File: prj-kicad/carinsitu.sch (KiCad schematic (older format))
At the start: 25 parts, among them P1 BAT, P2 MOT, U1 ESP32, U2 MIC2860, X1 40MHz

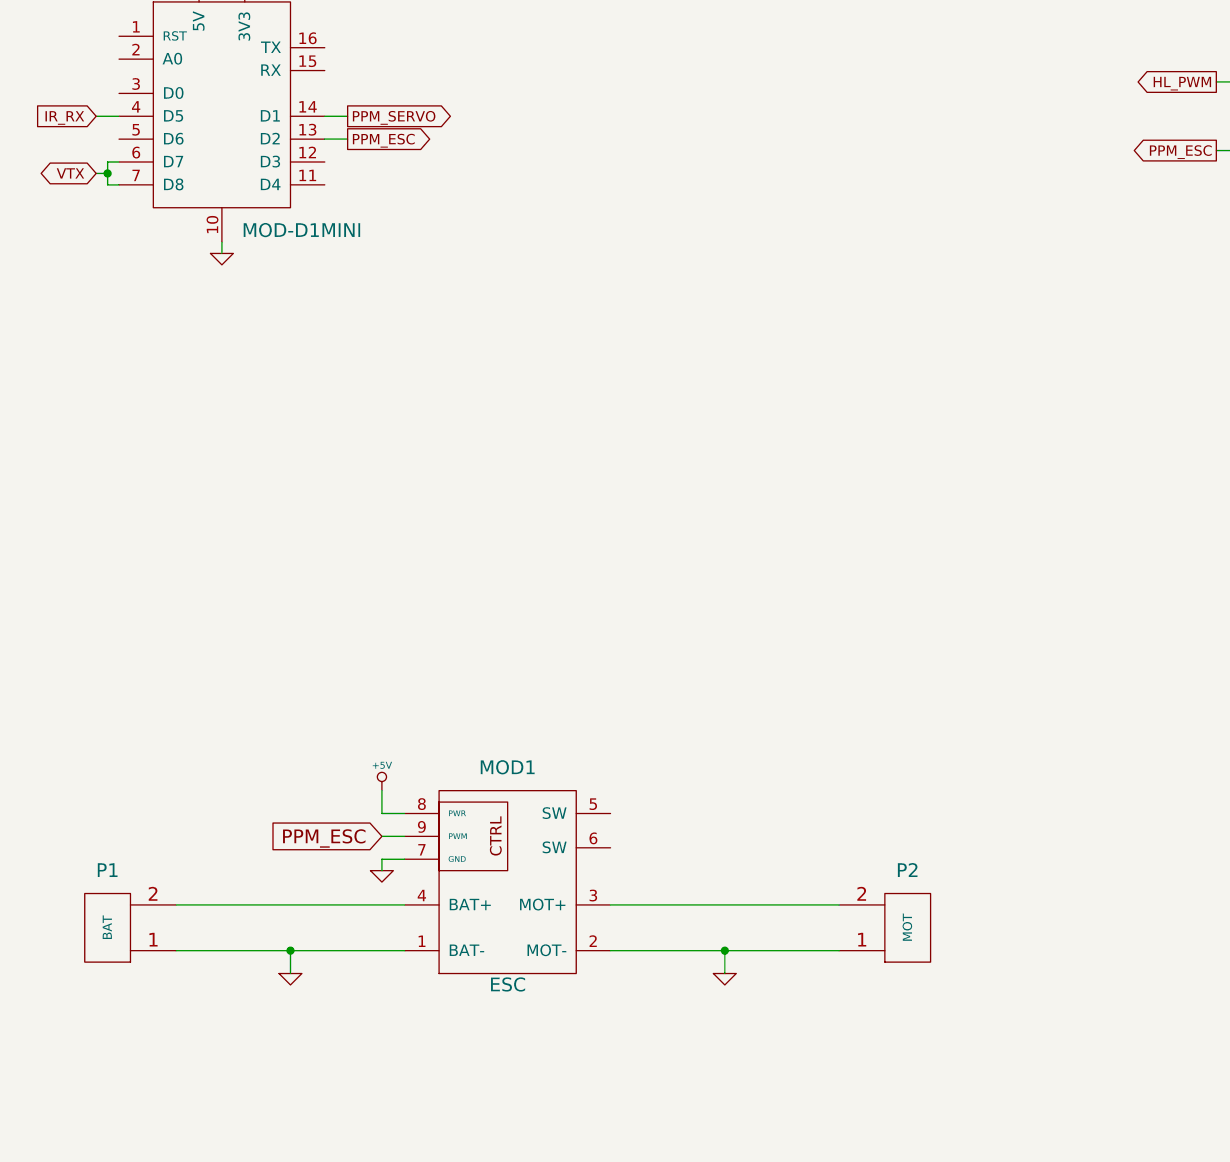
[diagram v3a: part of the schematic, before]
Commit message: = ADD: Insert a slide switch to connect power (on / off)
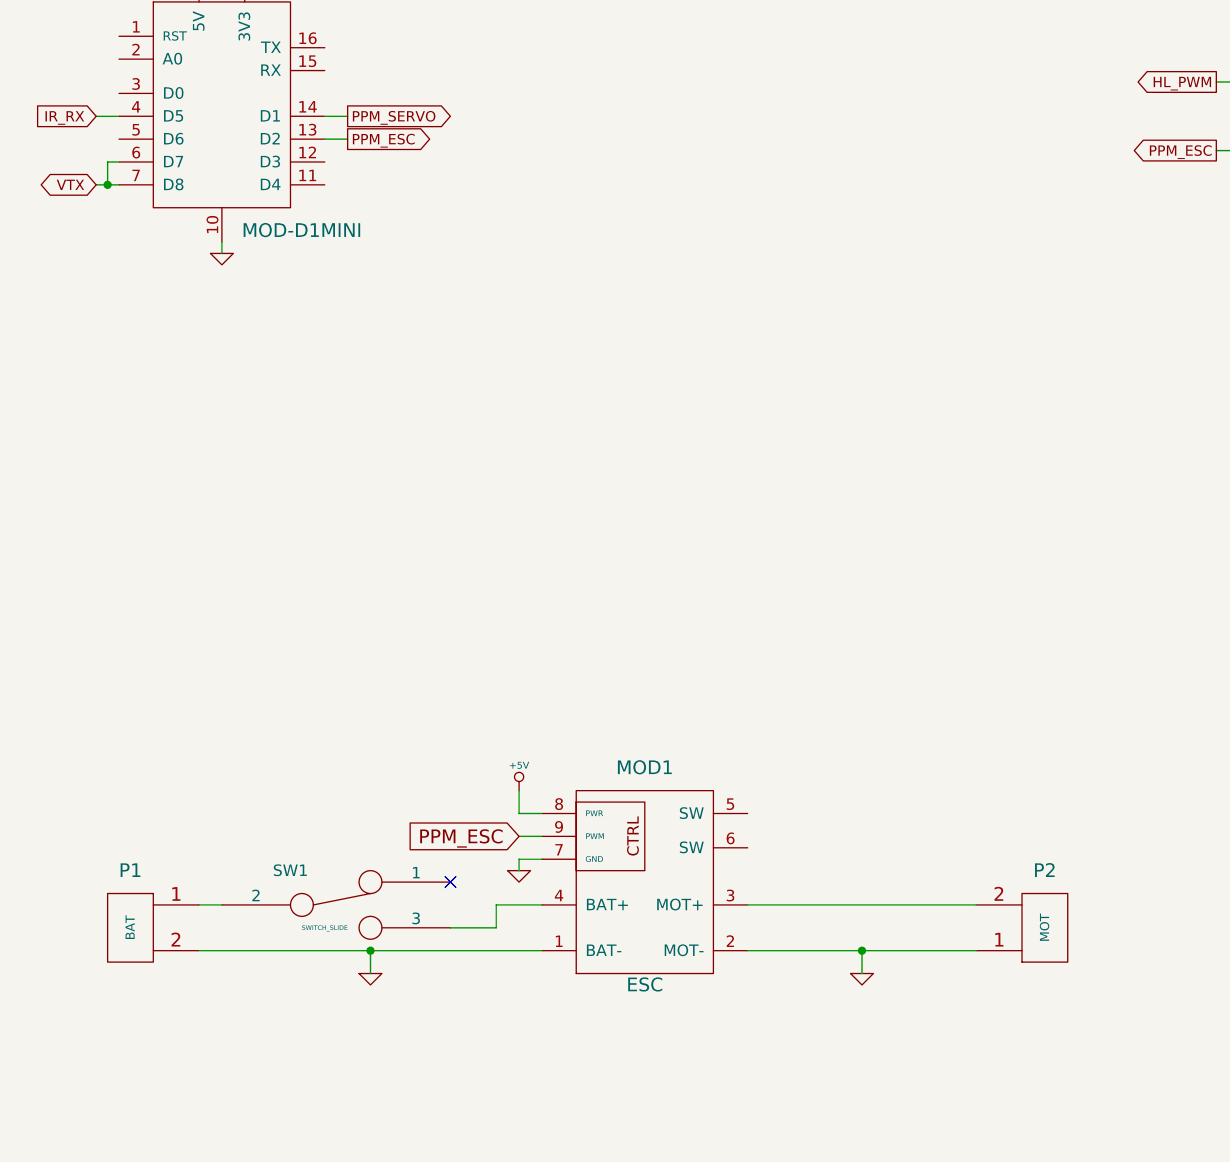
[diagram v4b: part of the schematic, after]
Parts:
- added SW1: SWITCH_SLIDE, carinsitu:SW_L102xxxML, symbol SWITCH_SLIDE
- U1: footprint (none) -> carinsitu:QFN48-04
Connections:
- net GND: now also P1.2 (PM); no longer P1.1 (P1)
- net at MOD1.4 (BAT+): now also SW1.3; no longer P1.2 (PM)
- new net: P1.1 (P1), SW1.2
- no-connect marks 4 -> 5
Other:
- moved on the sheet: MOD1, P1, P2

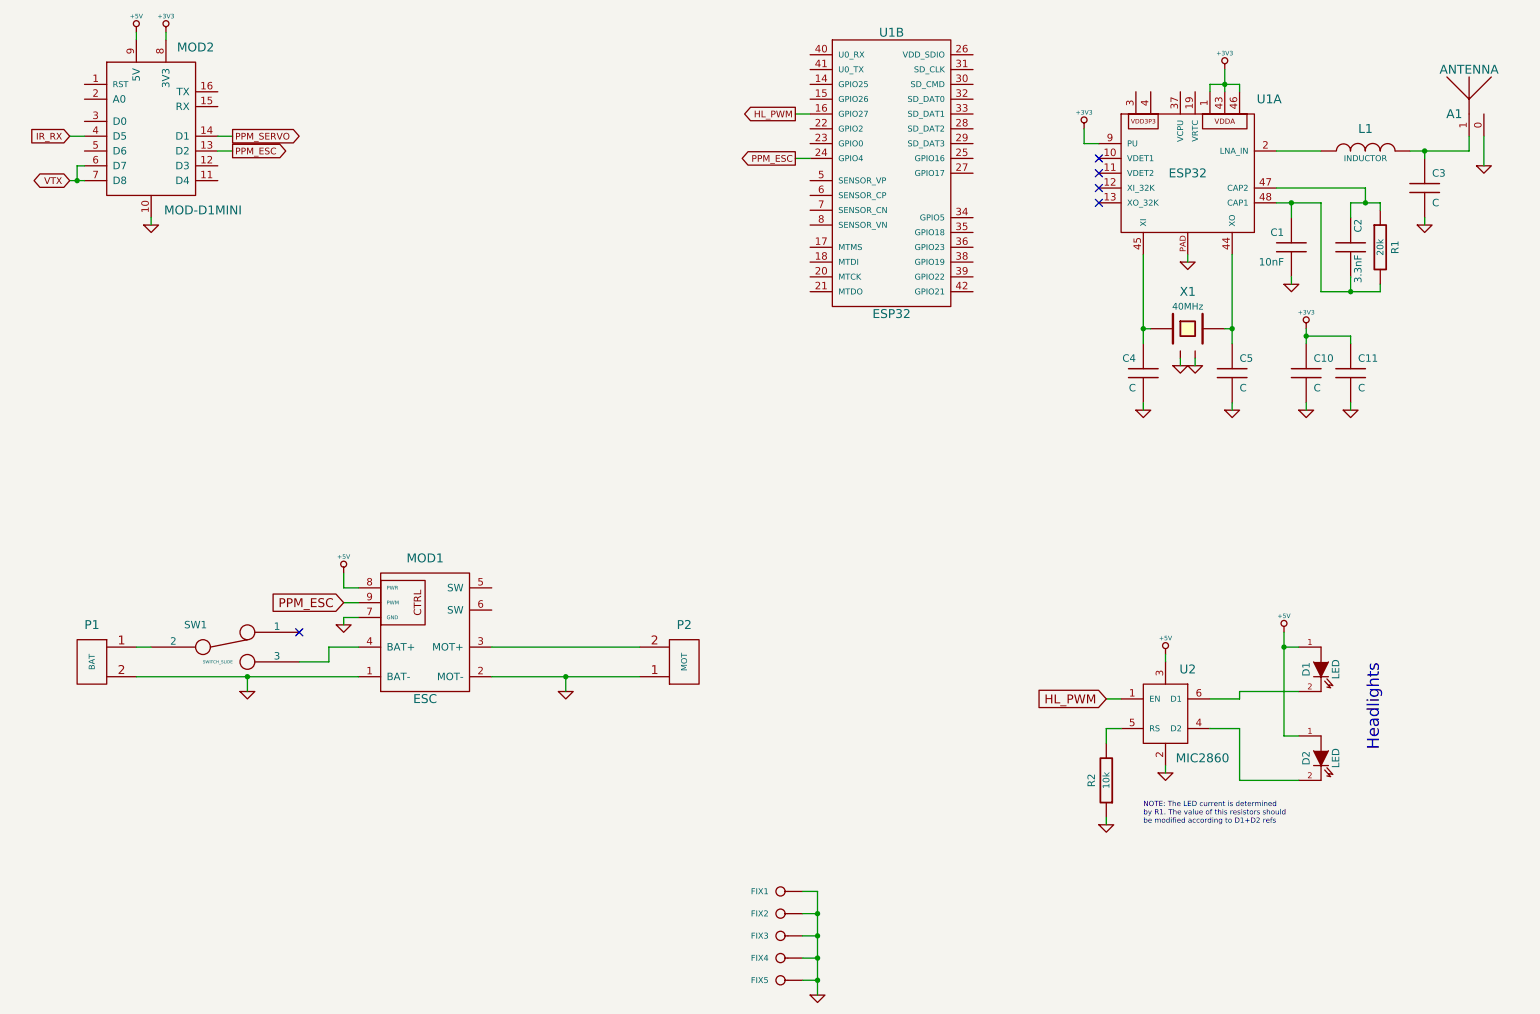
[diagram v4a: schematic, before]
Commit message: = ADD: Insert battery monitor (STC3100)
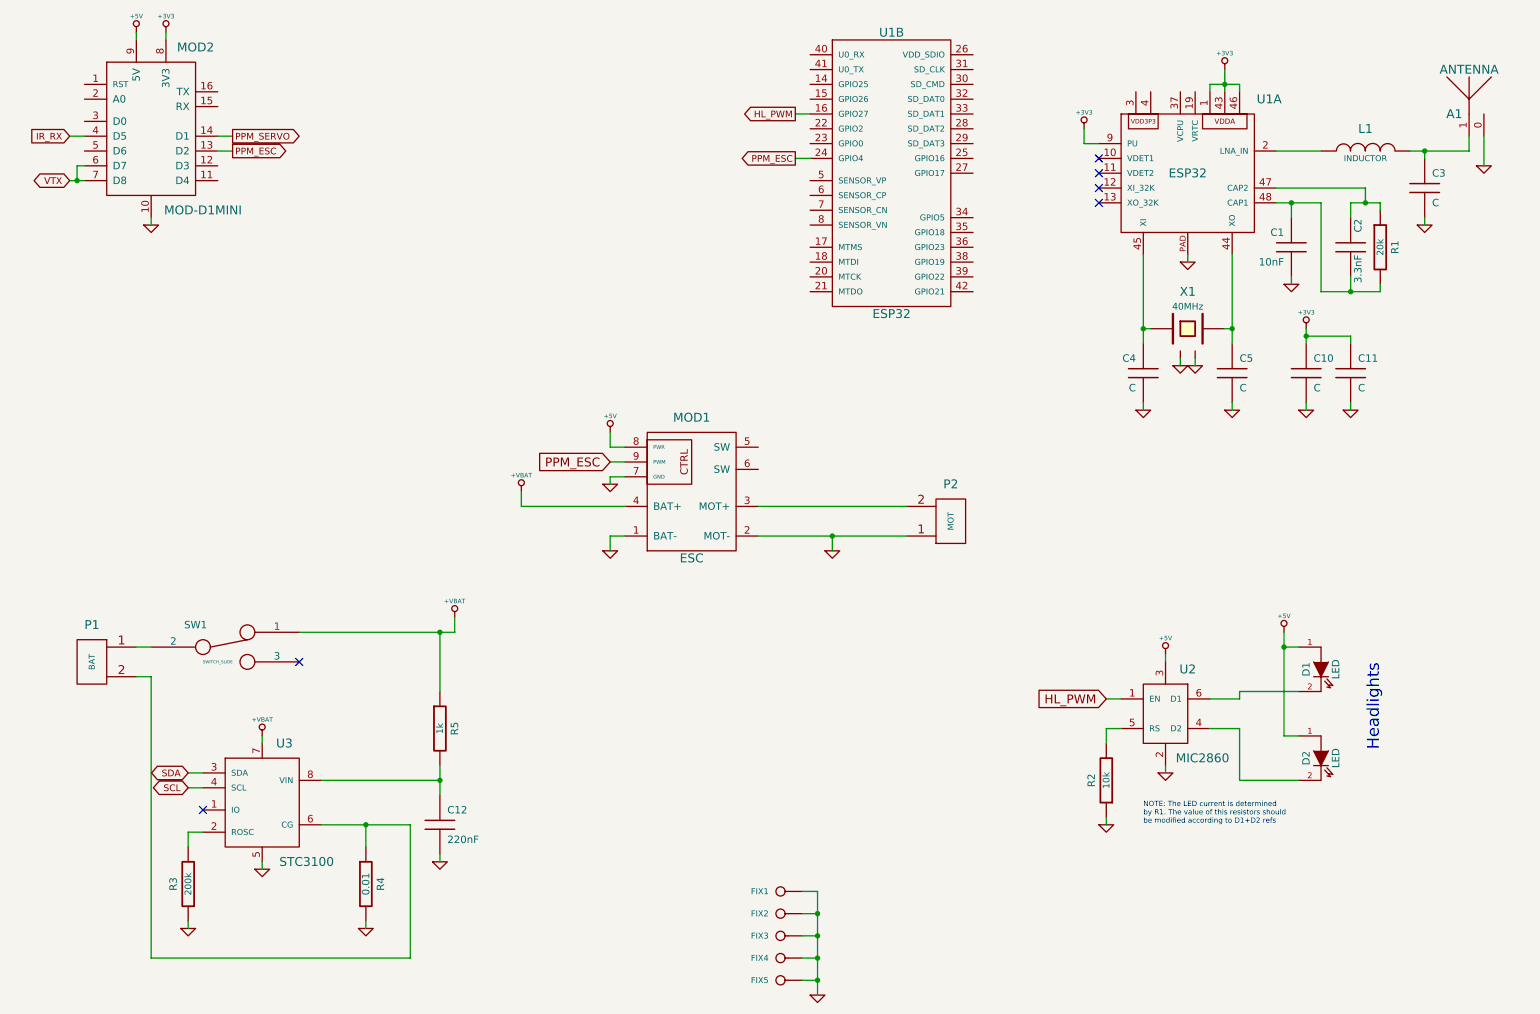
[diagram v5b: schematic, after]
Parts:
- added C12: 220nF, carinsitu:SMD0603, symbol C
- added R3: 200k, carinsitu:SMD0603, symbol R
- added R4: 0.01, carinsitu:SMD0805, symbol R
- added R5: 1k, carinsitu:SMD0603, symbol R
- added U3: STC3100, carinsitu:MSOP-8, symbol STC3100
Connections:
- net GND: now also C12.2, R3.1, R4.2, U3.5; no longer P1.2 (PM)
- net at SW1.3: no longer MOD1.4 (BAT+)
- net +VBAT: now reaches SW1.1
- net +VBAT: now also MOD1.4 (BAT+), R5.1, U3.7
- new net: P1.2 (PM), R4.1, U3.6 (CG)
- new net: R3.2, U3.2 (ROSC)
- new net: C12.1, R5.2, U3.8 (VIN)
- new net SCL: U3.4 (SCL)
- new net SDA: U3.3 (SDA)
- no-connect marks 5 -> 6
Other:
- moved on the sheet: MOD1, P2

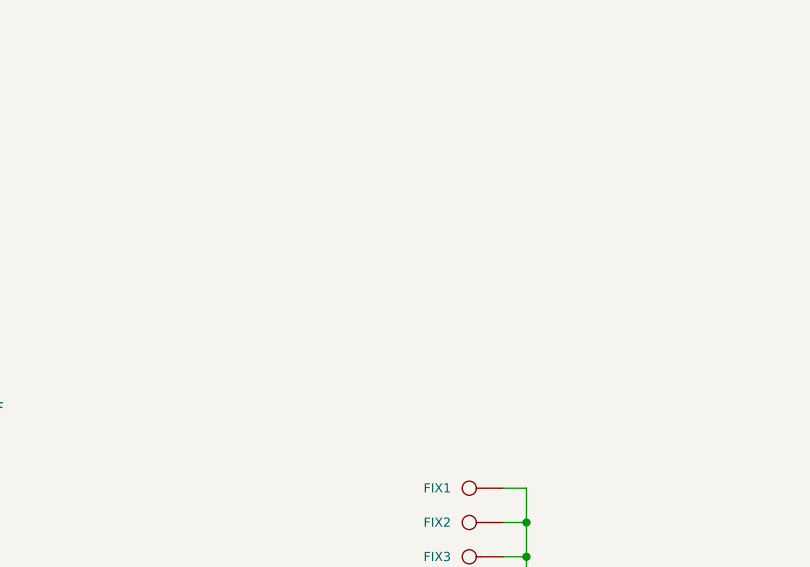
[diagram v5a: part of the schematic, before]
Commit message: = ADD: insert a 3 pin connector for servo (direction)
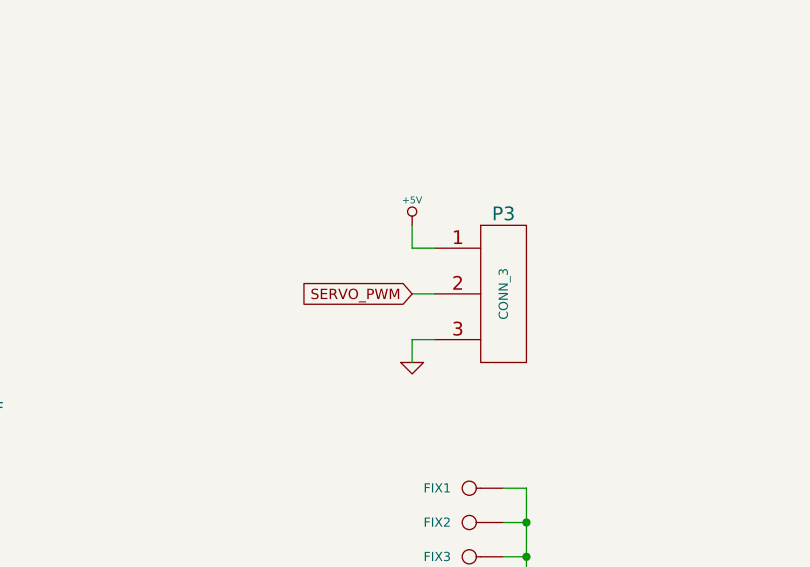
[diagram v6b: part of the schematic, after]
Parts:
- added P3: CONN_3, carinsitu:CONN_61300311021, symbol CONN_3
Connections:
- net +5V: now also P3.1 (P1)
- net GND: now also P3.3 (P3)
- new net SERVO_PWM: P3.2 (P2)
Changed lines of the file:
@@
 	3750 6600 3750 6550
 Connection ~ 3750 5050
+$Comp
+L CONN_3 P3
+U 1 1 5D249759
+P 6200 5950
+F 0 "P3" H 6200 6300 60  0000 C CNN
+F 1 "CONN_3" V 6200 5950 40  0000 C CNN
+F 2 "carinsitu:CONN_61300311021" H 6200 5950 60  0001 C CNN
+F 3 "" H 6200 5950 60  0000 C CNN
+	1    6200 5950
+	1    0    0    -1
+$EndComp
+$Comp
+L +5V #PWR033
+U 1 1 5D249839
+P 5800 5650
+F 0 "#PWR033" H 5800 5610 30  0001 C CNN
+F 1 "+5V" H 5800 5760 30  0000 C CNN
+F 2 "" H 5800 5650 60  0000 C CNN
+F 3 "" H 5800 5650 60  0000 C CNN
+	1    5800 5650
+	1    0    0    -1
+$EndComp
+$Comp
+L GND #PWR034
+U 1 1 5D24995A
+P 5800 6250
+F 0 "#PWR034" H 5800 6250 30  0001 C CNN
+F 1 "GND" H 5800 6180 30  0001 C CNN
+F 2 "" H 5800 6250 60  0000 C CNN
+F 3 "" H 5800 6250 60  0000 C CNN
+	1    5800 6250
+	1    0    0    -1
+$EndComp
+Wire Wire Line
+	5800 6250 5800 6150
+Wire Wire Line
+	5800 6150 5900 6150
+Wire Wire Line
+	5900 5750 5800 5750
+Wire Wire Line
+	5800 5750 5800 5650
+Text GLabel 5800 5950 0    45   Input ~ 0
+SERVO_PWM
+Wire Wire Line
+	5800 5950 5900 5950
 $EndSCHEMATC

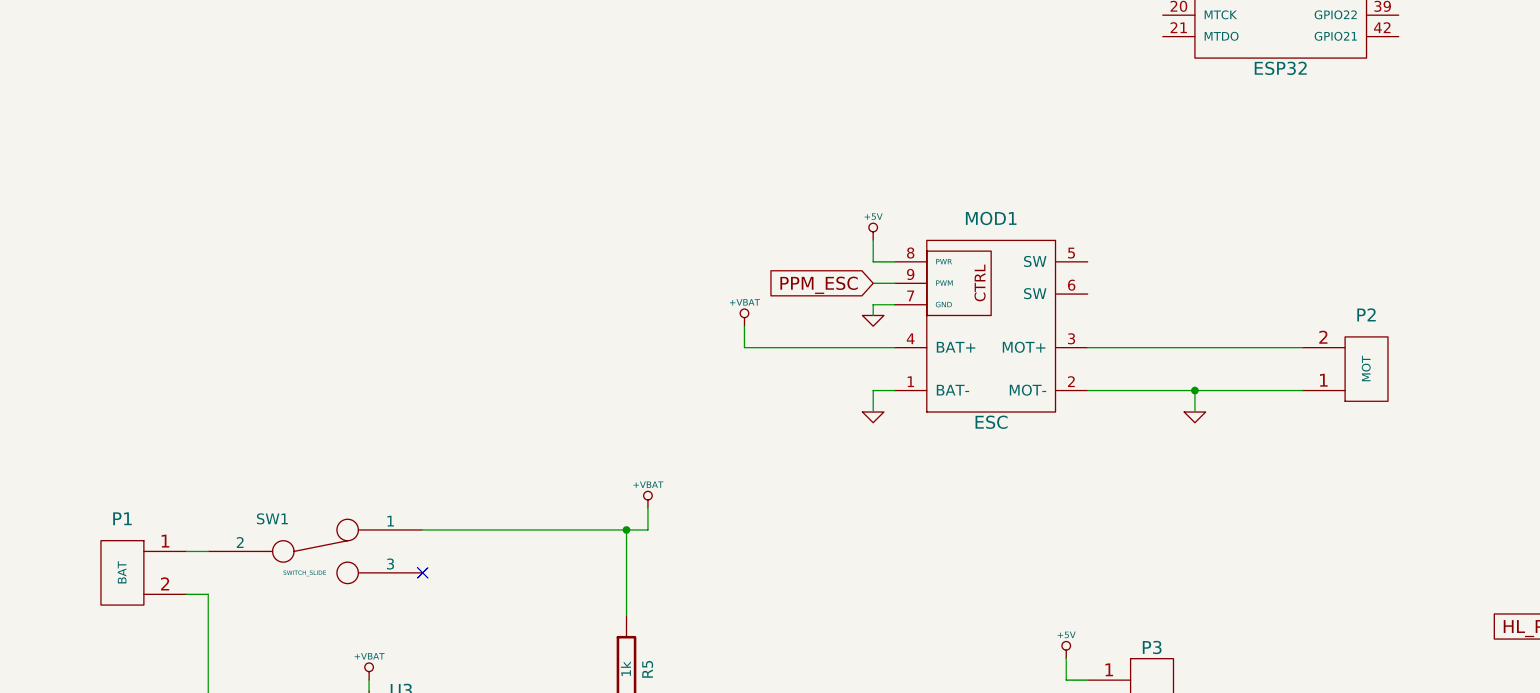
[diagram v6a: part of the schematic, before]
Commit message: = ADD: insert second RGB led and add a level switch (3V3 -> 5V) on data line
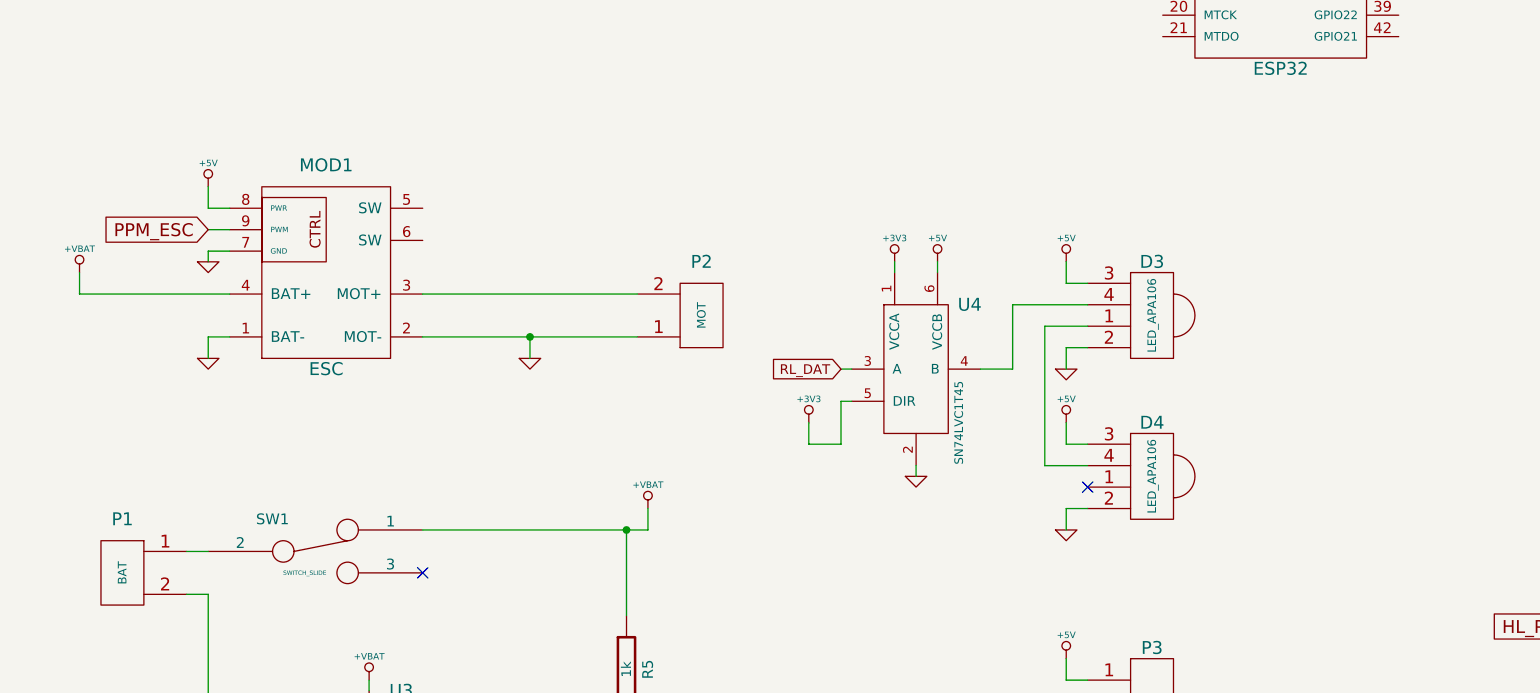
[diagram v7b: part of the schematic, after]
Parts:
- added D3, D4: LED_APA106, carinsitu:LED-APA106, symbol LED_APA106
- added U4: SN74LVC1T45, carinsitu:SOT23-6, symbol SN74LVC1T45
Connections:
- net +3V3: now also U4.1 (VCCA), U4.5 (DIR)
- net +5V: now also D3.3 (VDD), D4.3 (VDD), U4.6 (VCCB)
- net GND: now also D3.2 (GND), D4.2 (GND), U4.2
- new net: D3.1 (DOUT), D4.4 (DIN)
- new net: D3.4 (DIN), U4.4 (B)
- new net RL_DAT: U4.3 (A)
- no-connect marks 6 -> 7
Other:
- moved on the sheet: MOD1, P2
